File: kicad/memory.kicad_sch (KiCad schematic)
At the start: 14 parts, among them U10 TMS4416, U11 TMS4416, U12 TMS4416, U13 74HC157, U14 74HC157, U15 74HC04, U16 74HC32, U5 27128, U8 CY62256-70PC, U9 TMS4416

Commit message: Add caps and make initial placement
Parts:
- added C16, C17, C18, C19, C20, C21, C22, C23, C24, C25: 100n, Capacitor_THT:C_Disc_D5.0mm_W2.5mm_P2.50mm, symbol Device:C
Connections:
- net GND: now also C16.2, C17.2, C18.2, C19.2, C20.2, C21.2, C22.2, C23.2, C24.2, C25.2
- net VCC: now also C16.1, C17.1, C18.1, C19.1, C20.1, C21.1, C22.1, C23.1, C24.1, C25.1
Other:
- moved on the sheet: U15G, U16E

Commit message: Bugfixes, start routing
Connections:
- net GND: now also U5.20 (~{CE}); no longer U15.13, U5.22 (~{OE})
- net /ROMCS: now also U5.22 (~{OE}); no longer U5.20 (~{CE})
- net at U13.1 (S), U14.1 (S): now also U15.12; no longer U15.6, U15.9
- new net: U15.13, U15.6, U15.9
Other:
- moved on the sheet: U15F
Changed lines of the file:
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@@
 	)
 	(junction
+		(at 77.47 124.46)
+		(diameter 0)
+		(color 0 0 0 0)
+	)
+	(junction
 		(at 59.69 124.46)
 		(diameter 0)
@@
 	)
 	(junction
+		(at 154.94 124.46)
+		(diameter 0)
+		(color 0 0 0 0)
+	)
+	(junction
 		(at 204.47 21.59)
 		(diameter 0)
@@
 	)
 	(junction
-		(at 77.47 124.46)
-		(diameter 0)
-		(color 0 0 0 0)
-	)
-	(junction
 		(at 138.43 25.4)
 		(diameter 0)
@@
 	)
 	(junction
-		(at 154.94 124.46)
-		(diameter 0)
-		(color 0 0 0 0)
-	)
-	(junction
 		(at 222.25 82.55)
 		(diameter 0)
@@
 	(wire
 		(pts
-			(xy 50.8 91.44) (xy 52.07 91.44)
-		)
-		(stroke
-			(width 0)
-			(type default)
-		)
-	)
-	(wire
-		(pts
 			(xy 78.74 135.89) (xy 77.47 135.89)
 		)
@@
 	(wire
 		(pts
+			(xy 50.8 88.9) (xy 50.8 97.79)
+		)
+		(stroke
+			(width 0)
+			(type default)
+		)
+	)
+	(wire
+		(pts
 			(xy 62.23 97.79) (xy 62.23 96.52)
 		)
@@
 	(wire
 		(pts
-			(xy 273.05 102.87) (xy 279.4 102.87)
+			(xy 151.13 124.46) (xy 154.94 124.46)
 		)
 		(stroke
@@
 	(wire
 		(pts
-			(xy 133.35 156.21) (xy 203.2 156.21)
-		)
-		(stroke
-			(width 0)
-			(type default)
-		)
-	)
-	(wire
-		(pts
-			(xy 91.44 181.61) (xy 95.25 181.61)
+			(xy 273.05 102.87) (xy 279.4 102.87)
 		)
 		(stroke
@@
 	(wire
 		(pts
-			(xy 200.66 128.27) (xy 189.23 128.27)
+			(xy 133.35 156.21) (xy 203.2 156.21)
 		)
 		(stroke
@@
 	(wire
 		(pts
-			(xy 77.47 124.46) (xy 154.94 124.46)
+			(xy 91.44 181.61) (xy 95.25 181.61)
 		)
 		(stroke
@@
 	(wire
 		(pts
-			(xy 151.13 170.18) (xy 151.13 172.72)
+			(xy 200.66 128.27) (xy 189.23 128.27)
 		)
 		(stroke
@@
 	(wire
 		(pts
-			(xy 50.8 97.79) (xy 50.8 91.44)
-		)
-		(stroke
-			(width 0)
-			(type default)
-		)
-	)
-	(wire
-		(pts
 			(xy 207.01 102.87) (xy 212.09 102.87)
 		)
@@
 	(wire
 		(pts
+			(xy 50.8 88.9) (xy 52.07 88.9)
+		)
+		(stroke
+			(width 0)
+			(type default)
+		)
+	)
+	(wire
+		(pts
 			(xy 58.42 124.46) (xy 59.69 124.46)
 		)
@@
 	(wire
 		(pts
+			(xy 46.99 91.44) (xy 52.07 91.44)
+		)
+		(stroke
+			(width 0)
+			(type default)
+		)
+	)
+	(wire
+		(pts
 			(xy 116.84 158.75) (xy 243.84 158.75)
 		)
@@
 	(wire
 		(pts
+			(xy 77.47 124.46) (xy 135.89 124.46)
+		)
+		(stroke
+			(width 0)
+			(type default)
+		)
+	)
+	(wire
+		(pts
 			(xy 72.39 58.42) (xy 78.74 58.42)
 		)
@@
 		)
 	)
-	(wire
-		(pts
-			(xy 46.99 88.9) (xy 52.07 88.9)
-		)
-		(stroke
-			(width 0)
-			(type default)
-		)
-	)
 	(bus
 		(pts
@@
 		)
 	)
-	(wire
-		(pts
-			(xy 152.4 170.18) (xy 151.13 170.18)
-		)
-		(stroke
-			(width 0)
-			(type default)
-		)
-	)
 	(bus
 		(pts
@@
 	(hierarchical_label "{slash}ROMCS"
 		(shape input)
-		(at 46.99 88.9 180)
+		(at 46.99 91.44 180)
 		(fields_autoplaced yes)
 		(effects
@@
 	)
 	(symbol
-		(lib_id "power:GND")
-		(at 151.13 172.72 0)
-		(unit 1)
-		(exclude_from_sim no)
-		(in_bom yes)
-		(on_board yes)
-		(dnp no)
-		(fields_autoplaced yes)
-		(property "Reference" "#PWR044"
-			(at 151.13 179.07 0)
-			(effects
-				(font
-					(size 1.27 1.27)
-				)
-				(hide yes)
-			)
-		)
-		(property "Value" "GND"
-			(at 151.13 177.8 0)
-			(effects
-				(font
-					(size 1.27 1.27)
-				)
-			)
-		)
-		(property "Footprint" ""
-			(at 151.13 172.72 0)
-			(effects
-				(font
-					(size 1.27 1.27)
-				)
-				(hide yes)
-			)
-		)
-		(property "Datasheet" ""
-			(at 151.13 172.72 0)
-			(effects
-				(font
-					(size 1.27 1.27)
-				)
-				(hide yes)
-			)
-		)
-		(property "Description" "Power symbol creates a global label with name \"GND\" , ground"
-			(at 151.13 172.72 0)
-			(effects
-				(font
-					(size 1.27 1.27)
-				)
-				(hide yes)
-			)
-		)
-		(pin "1"
-		)
-		(instances
-			(project "fella"
-				(path "/0e49b66d-39aa-4a48-b9a1-8037366b6d94/69d6a2d5-bbb3-4608-ab8d-5d0d29ae2e94"
-					(reference "#PWR044")
-					(unit 1)
-				)
-			)
-		)
-	)
-	(symbol
 		(lib_id "Device:C")
 		(at 54.61 176.53 0)
@@
 	(symbol
 		(lib_id "74xx:74HC04")
-		(at 160.02 170.18 0)
+		(at 143.51 124.46 0)
 		(unit 6)
 		(exclude_from_sim no)
@@
 		(on_board yes)
 		(dnp no)
-		(fields_autoplaced yes)
 		(property "Reference" "U15"
-			(at 160.02 161.29 0)
+			(at 146.558 120.65 0)
 			(effects
 				(font
@@
 		)
 		(property "Value" "74HC04"
-			(at 160.02 163.83 0)
+			(at 147.574 127.762 0)
 			(effects
 				(font
@@
 		)
 		(property "Footprint" "Package_DIP:DIP-14_W7.62mm"
-			(at 160.02 170.18 0)
+			(at 143.51 124.46 0)
 			(effects
 				(font
@@
 		)
 		(property "Datasheet" "https://assets.nexperia.com/documents/data-sheet/74HC_HCT04.pdf"
-			(at 160.02 170.18 0)
+			(at 143.51 124.46 0)
 			(effects
 				(font
@@
 		)
 		(property "Description" "Hex Inverter"
-			(at 160.02 170.18 0)
+			(at 143.51 124.46 0)
 			(effects
 				(font

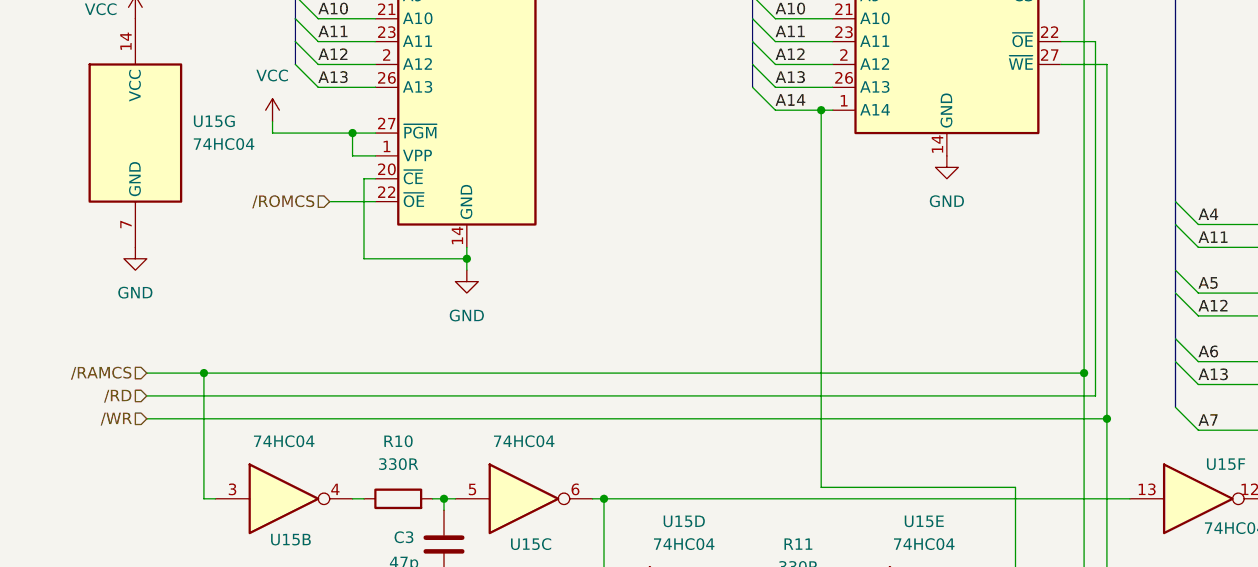
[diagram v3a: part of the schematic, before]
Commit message: Finished routing, HW prototype ready
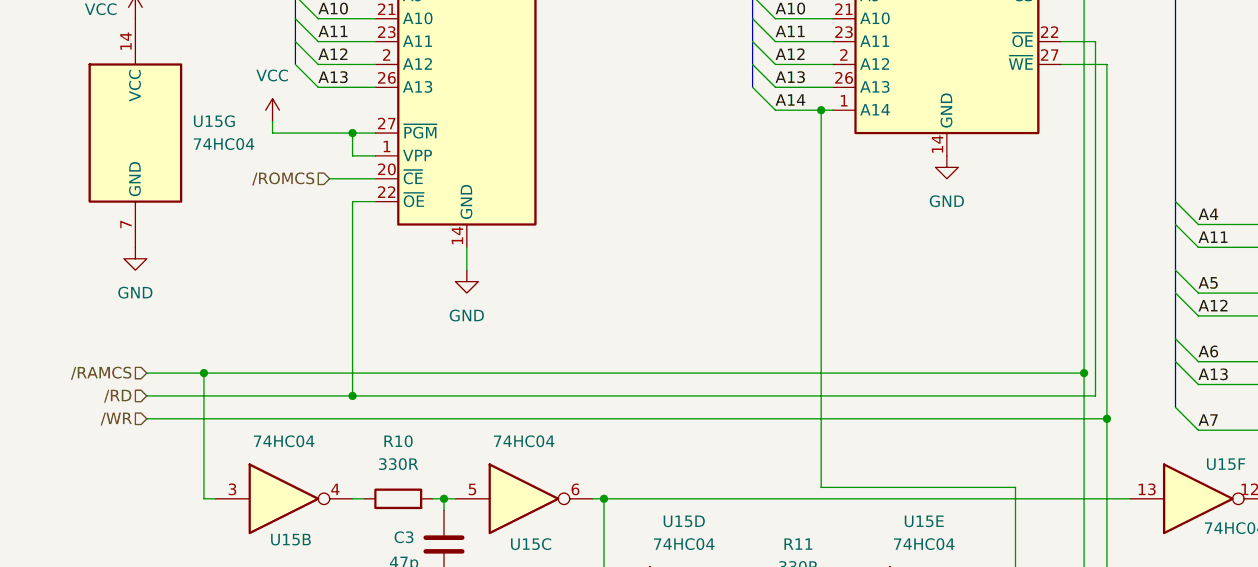
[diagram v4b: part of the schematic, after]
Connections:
- net GND: no longer U5.20 (~{CE})
- net /RD: now also U5.22 (~{OE})
- net /ROMCS: now also U5.20 (~{CE}); no longer U5.22 (~{OE})
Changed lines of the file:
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@@
 	)
 	(junction
-		(at 62.23 97.79)
+		(at 203.2 135.89)
 		(diameter 0)
 		(color 0 0 0 0)
 	)
 	(junction
-		(at 203.2 135.89)
+		(at 125.73 189.23)
 		(diameter 0)
 		(color 0 0 0 0)
 	)
 	(junction
-		(at 125.73 189.23)
+		(at 49.53 113.03)
 		(diameter 0)
 		(color 0 0 0 0)
@@
 	(wire
 		(pts
-			(xy 26.67 113.03) (xy 132.08 113.03)
+			(xy 26.67 113.03) (xy 49.53 113.03)
 		)
 		(stroke
@@
 	(wire
 		(pts
-			(xy 50.8 88.9) (xy 50.8 97.79)
-		)
-		(stroke
-			(width 0)
-			(type default)
-		)
-	)
-	(wire
-		(pts
-			(xy 62.23 97.79) (xy 62.23 96.52)
+			(xy 62.23 96.52) (xy 62.23 99.06)
 		)
 		(stroke
@@
 	(wire
 		(pts
-			(xy 50.8 88.9) (xy 52.07 88.9)
+			(xy 58.42 124.46) (xy 59.69 124.46)
 		)
 		(stroke
@@
 	(wire
 		(pts
-			(xy 58.42 124.46) (xy 59.69 124.46)
+			(xy 168.91 134.62) (xy 168.91 135.89)
 		)
 		(stroke
@@
 	(wire
 		(pts
-			(xy 168.91 134.62) (xy 168.91 135.89)
+			(xy 262.89 143.51) (xy 262.89 144.78)
 		)
 		(stroke
@@
 	(wire
 		(pts
-			(xy 262.89 143.51) (xy 262.89 144.78)
+			(xy 49.53 91.44) (xy 49.53 113.03)
 		)
 		(stroke
@@
 		)
 	)
+	(wire
+		(pts
+			(xy 49.53 113.03) (xy 132.08 113.03)
+		)
+		(stroke
+			(width 0)
+			(type default)
+		)
+	)
 	(bus
 		(pts
@@
 	(wire
 		(pts
-			(xy 62.23 97.79) (xy 50.8 97.79)
-		)
-		(stroke
-			(width 0)
-			(type default)
-		)
-	)
-	(wire
-		(pts
 			(xy 133.35 115.57) (xy 133.35 76.2)
 		)
@@
 	(wire
 		(pts
-			(xy 46.99 91.44) (xy 52.07 91.44)
+			(xy 116.84 158.75) (xy 243.84 158.75)
 		)
 		(stroke
@@
 	(wire
 		(pts
-			(xy 116.84 158.75) (xy 243.84 158.75)
+			(xy 60.96 124.46) (xy 59.69 124.46)
 		)
 		(stroke
@@
 	(wire
 		(pts
-			(xy 60.96 124.46) (xy 59.69 124.46)
+			(xy 212.09 130.81) (xy 201.93 130.81)
 		)
 		(stroke
@@
 	(wire
 		(pts
-			(xy 212.09 130.81) (xy 201.93 130.81)
+			(xy 46.99 88.9) (xy 52.07 88.9)
 		)
 		(stroke
@@
 		)
 	)
+	(wire
+		(pts
+			(xy 52.07 91.44) (xy 49.53 91.44)
+		)
+		(stroke
+			(width 0)
+			(type default)
+		)
+	)
 	(bus
 		(pts
@@
 		)
 	)
-	(wire
-		(pts
-			(xy 62.23 99.06) (xy 62.23 97.79)
-		)
-		(stroke
-			(width 0)
-			(type default)
-		)
-	)
 	(bus
 		(pts
@@
 	(hierarchical_label "{slash}ROMCS"
 		(shape input)
-		(at 46.99 91.44 180)
+		(at 46.99 88.9 180)
 		(fields_autoplaced yes)
 		(effects

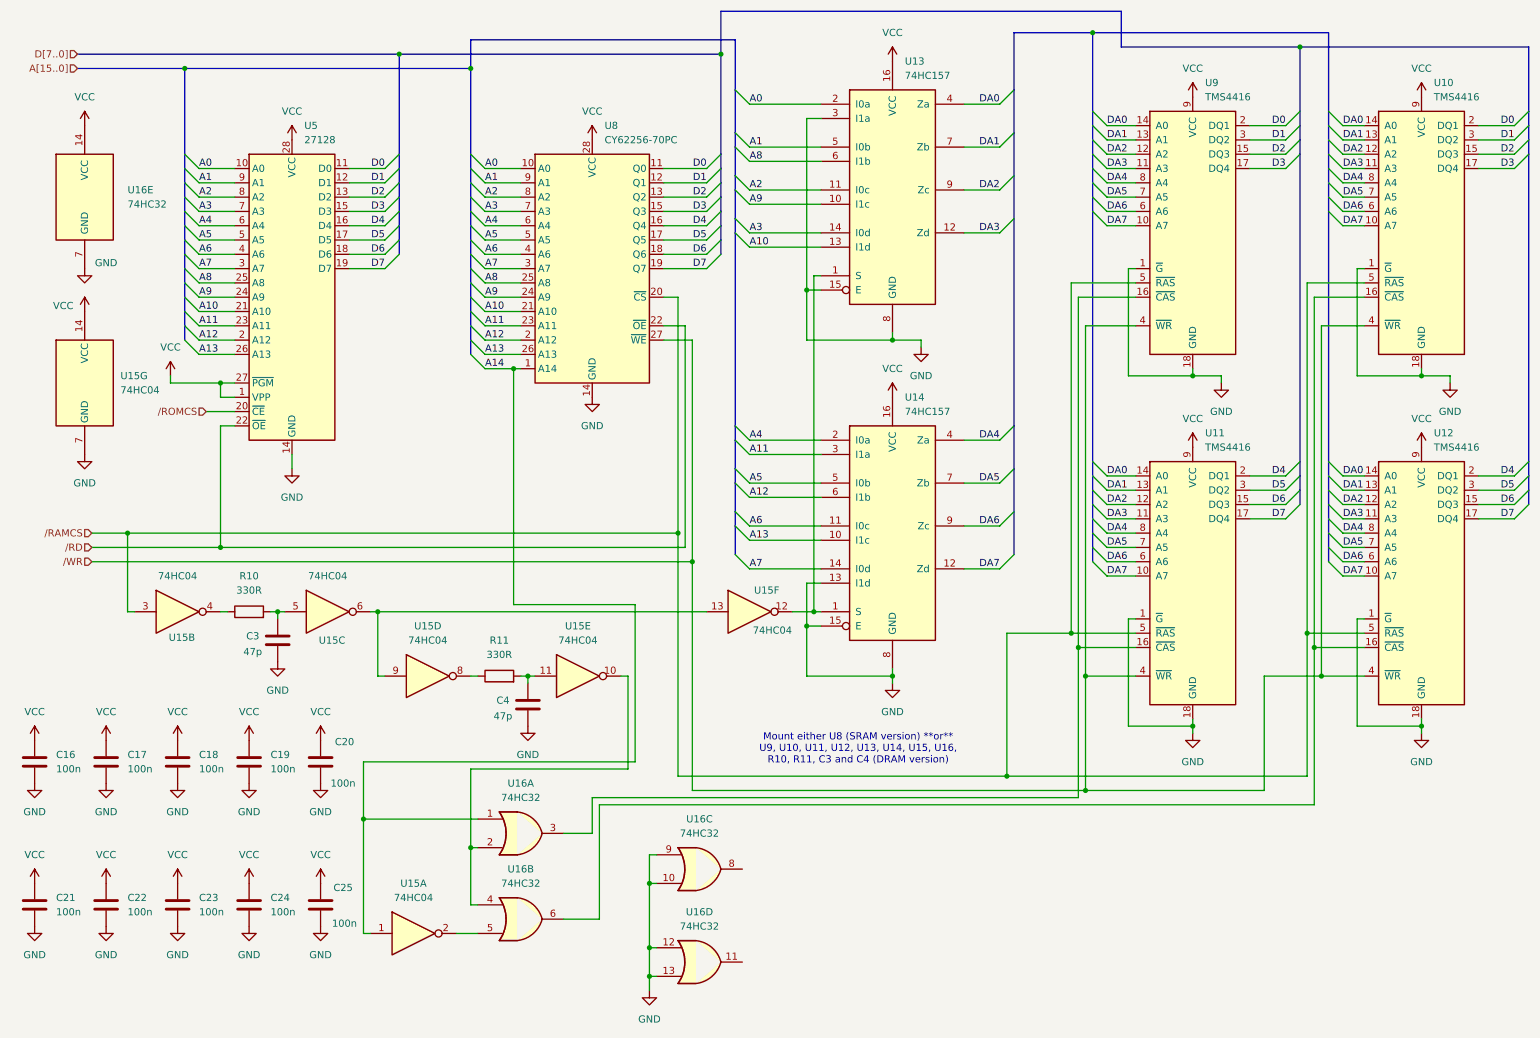
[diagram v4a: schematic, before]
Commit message: hw: revision C
Major changes:
- ROM space has been extended from 16 KiB to 32 KiB
- dynamic RAM option has been removed
- RAM size has been reduced from 32 KiB to 24 KiB
- expansion slot now replaces internal ROM, does not
  have dedicated memory space anymore
- place all I/O within a compactish 8 KiB
- move PH2 gating to /RD and /WR signals
- PCB redo (mechanicaly compatible)
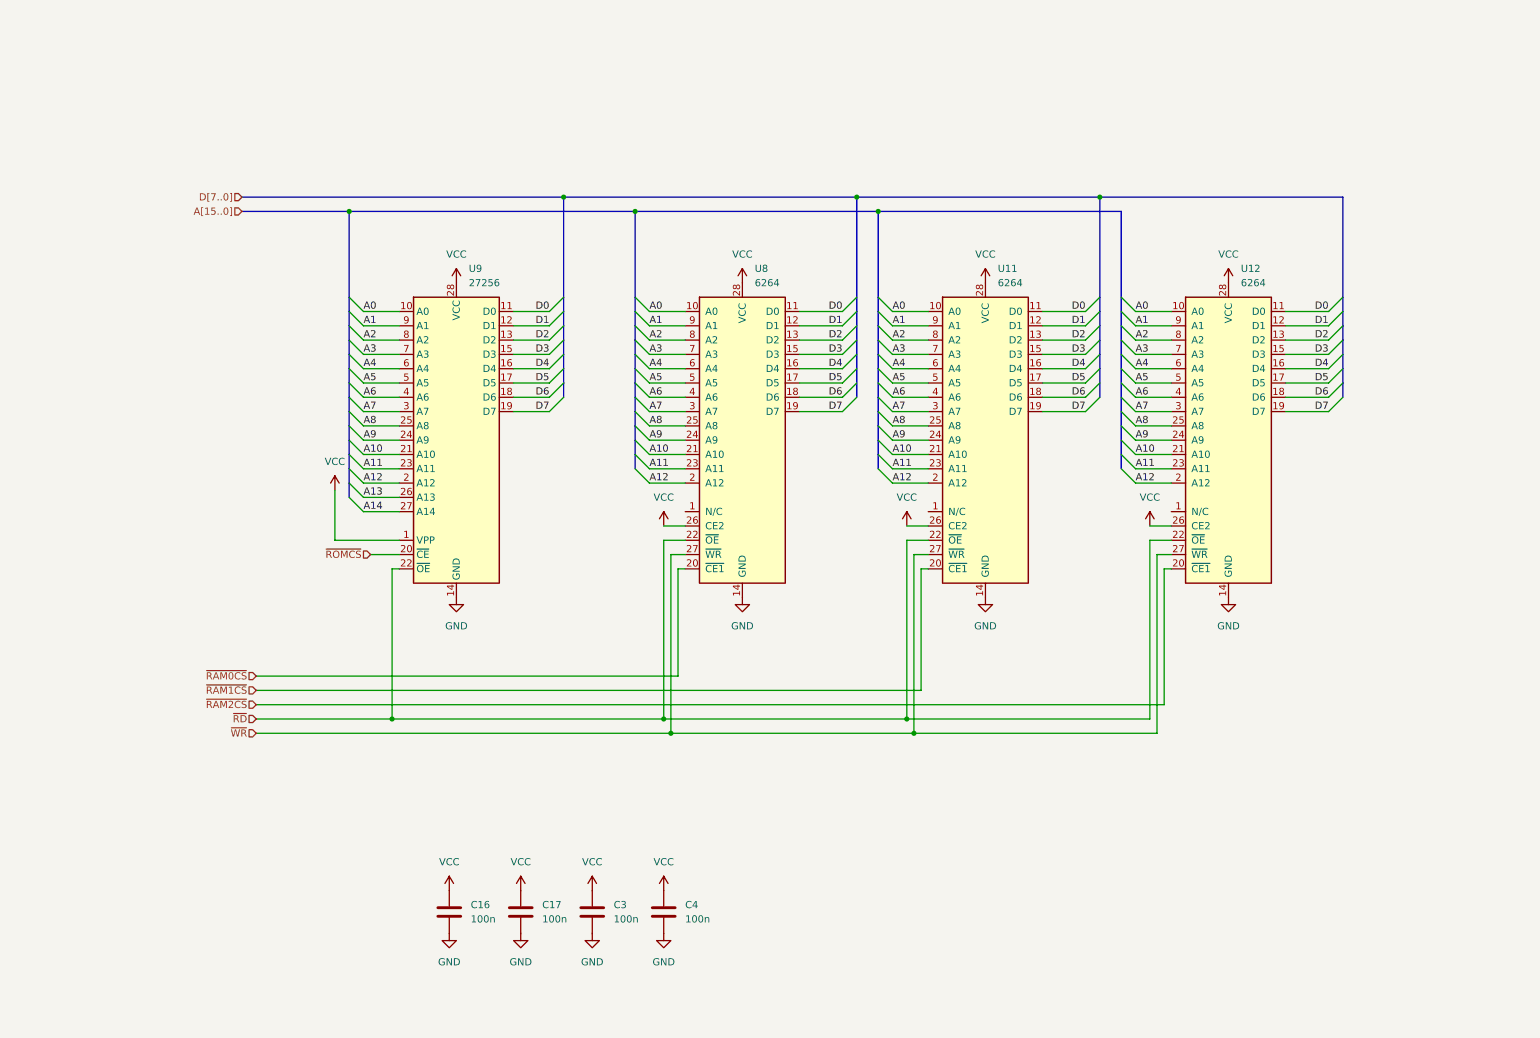
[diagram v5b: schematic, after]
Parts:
- removed C18, C19, C20, C21, C22, C23, C24, C25: 100n, Capacitor_THT:C_Disc_D5.0mm_W2.5mm_P2.50mm, symbol Device:C
- removed R10, R11: 330R, Resistor_THT:R_Axial_DIN0207_L6.3mm_D2.5mm_P7.62mm_Horizontal, symbol Device:R
- removed U10, U11, U12, U9: TMS4416, Package_DIP:DIP-18_W7.62mm, symbol 8bits:TMS4416
- removed U13, U14: 74HC157, Package_DIP:DIP-16_W7.62mm, symbol 74xx:74LS157
- removed U15: 74HC04, Package_DIP:DIP-14_W7.62mm, symbol 74xx:74HC04
- removed U16: 74HC32, Package_DIP:DIP-14_W7.62mm, symbol 74xx:74LS32
- removed U5: 27128, Package_DIP:DIP-28_W15.24mm, symbol Memory_EPROM:27128
- removed U8: CY62256-70PC, Package_DIP:DIP-28_W15.24mm, symbol Memory_RAM:CY62256-70PC
- added U11, U12, U8: 6264, Package_DIP:DIP-28_W15.24mm, symbol 8bits:6264
- added U9: 27256, Package_DIP:DIP-28_W15.24mm, symbol Memory_EPROM:27256
- C3, C4: value 47p -> 100n
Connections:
- net A0: now also U11.10 (A0), U12.10 (A0), U8.10 (A0), U9.10 (A0)
- net A1: now also U11.9 (A1), U12.9 (A1), U8.9 (A1), U9.9 (A1)
- net A10: now also U11.21 (A10), U12.21 (A10), U8.21 (A10), U9.21 (A10)
- net A11: now also U11.23 (A11), U12.23 (A11), U8.23 (A11), U9.23 (A11)
- net A12: now also U11.2 (A12), U12.2 (A12), U8.2 (A12), U9.2 (A12)
- net A13: now also U9.26 (A13)
- net A14: now also U9.27 (A14)
- net A2: now also U11.8 (A2), U12.8 (A2), U8.8 (A2), U9.8 (A2)
- net A3: now also U11.7 (A3), U12.7 (A3), U8.7 (A3), U9.7 (A3)
- net A4: now also U11.6 (A4), U12.6 (A4), U8.6 (A4), U9.6 (A4)
- net A5: now also U11.5 (A5), U12.5 (A5), U8.5 (A5), U9.5 (A5)
- net A6: now also U11.4 (A6), U12.4 (A6), U8.4 (A6), U9.4 (A6)
- net A7: now also U11.3 (A7), U12.3 (A7), U8.3 (A7), U9.3 (A7)
- net A8: now also U11.25 (A8), U12.25 (A8), U8.25 (A8), U9.25 (A8)
- net A9: now also U11.24 (A9), U12.24 (A9), U8.24 (A9), U9.24 (A9)
- net D0: now also U11.11 (D0), U12.11 (D0), U8.11 (D0), U9.11 (D0)
- net D1: now also U11.12 (D1), U12.12 (D1), U8.12 (D1), U9.12 (D1)
- net D2: now also U11.13 (D2), U12.13 (D2), U8.13 (D2), U9.13 (D2)
- net D3: now also U11.15 (D3), U12.15 (D3), U8.15 (D3), U9.15 (D3)
- net D4: now also U11.16 (D4), U12.16 (D4), U8.16 (D4), U9.16 (D4)
- net D5: now also U11.17 (D5), U12.17 (D5), U8.17 (D5), U9.17 (D5)
- net D6: now also U11.18 (D6), U12.18 (D6), U8.18 (D6), U9.18 (D6)
- net D7: now also U11.19 (D7), U12.19 (D7), U8.19 (D7), U9.19 (D7)
- net GND: now also U11.14 (GND), U12.14 (GND), U8.14 (GND), U9.14 (GND)
- net VCC: now also C3.1, C4.1, U11.26 (CE2), U11.28 (VCC), U12.26 (CE2), U12.28 (VCC), U8.26 (CE2), U8.28 (VCC), U9.1 (VPP), U9.28 (VCC)
- new net ~{RAM0CS}: U8.20 (~{CE1})
- new net ~{RAM1CS}: U11.20 (~{CE1})
- new net ~{RAM2CS}: U12.20 (~{CE1})
- new net ~{RD}: U11.22 (~{OE}), U12.22 (~{OE}), U8.22 (~{OE}), U9.22 (~{OE})
- new net ~{ROMCS}: U9.20 (~{CE})
- new net ~{WR}: U11.27 (~{WR}), U12.27 (~{WR}), U8.27 (~{WR})
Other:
- note removed: "Mount either U8 (SRAM version) **or** U9, U10, U11, U12, U13, U14, U15, U16, R10, R11, C3 and C4 (DRAM version)"
- moved on the sheet: C16, C17

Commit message: hw: rev D - replace DB25 connector footprint with available one
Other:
- company: (none) -> A.K.
- title: (none) -> Memory
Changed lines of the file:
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@@
 (kicad_sch
-	(version 20231120)
+	(version 20250114)
 	(generator "eeschema")
-	(generator_version "8.0")
+	(generator_version "9.0")
 	(paper "A4")
+	(title_block
+		(title "Memory")
+		(date "2025-08-04")
+		(rev "D")
+		(company "A.K.")
+	)
 	(junction
 		(at 171.45 143.51)
